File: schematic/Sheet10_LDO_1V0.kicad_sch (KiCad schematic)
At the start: 8 parts, among them U8 TPS7H1111-SP

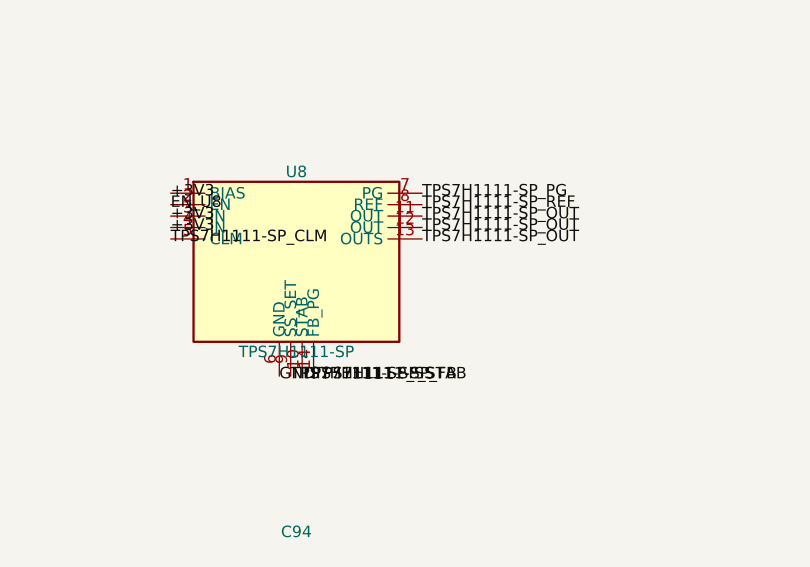
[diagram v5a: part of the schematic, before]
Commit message: fix: isolate ISL70003ASEH buck pins, fix LMX_SYNC collision, NC pins, connector pin names
- ISL70003ASEH pins now use ref prefix (U6_LX1 vs U7_LX1) to prevent shorts
- Buck SYNC pins separated from LMX_SYNC (power sync ≠ PLL sync)
- NC pins properly skipped (unconnected)
- Connector PIN_1..PIN_6 use ref prefix (J1_PIN_1 vs J2_PIN_1)
- Fixed annotation warnings in Sheet13 (C_dev→C125, R_dev→R74, U_TPS7H→U14)
- Regenerated all PDFs and SVGs
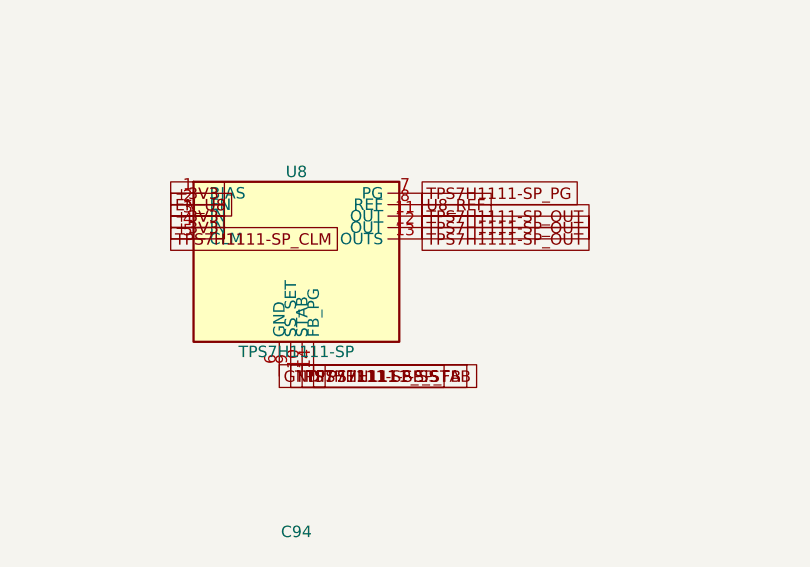
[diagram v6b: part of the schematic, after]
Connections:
- net TPS7H1111-SP_REF renamed U8_REF
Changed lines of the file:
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@@
     (pin "2")
   )
-  (label "+3V3" (at 186.0300 72.3800 0) (effects (font (size 1.27 1.27))))
-  (label "EN_U8" (at 186.0300 73.6500 0) (effects (font (size 1.27 1.27))))
-  (label "+3V3" (at 186.0300 74.9200 0) (effects (font (size 1.27 1.27))))
-  (label "+3V3" (at 186.0300 76.1900 0) (effects (font (size 1.27 1.27))))
-  (label "TPS7H1111-SP_CLM" (at 186.0300 77.4600 0) (effects (font (size 1.27 1.27))))
-  (label "TPS7H1111-SP_PG" (at 213.9700 72.3800 0) (effects (font (size 1.27 1.27))))
-  (label "TPS7H1111-SP_REF" (at 213.9700 73.6500 0) (effects (font (size 1.27 1.27))))
-  (label "TPS7H1111-SP_OUT" (at 213.9700 74.9200 0) (effects (font (size 1.27 1.27))))
-  (label "TPS7H1111-SP_OUT" (at 213.9700 76.1900 0) (effects (font (size 1.27 1.27))))
-  (label "TPS7H1111-SP_OUT" (at 213.9700 77.4600 0) (effects (font (size 1.27 1.27))))
-  (label "GND" (at 198.0950 92.7000 0) (effects (font (size 1.27 1.27))))
-  (label "TPS7H1111-SP_SS" (at 199.3650 92.7000 0) (effects (font (size 1.27 1.27))))
-  (label "TPS7H1111-SP_STAB" (at 200.6350 92.7000 0) (effects (font (size 1.27 1.27))))
-  (label "TPS7H1111-SP_FB" (at 201.9050 92.7000 0) (effects (font (size 1.27 1.27))))
+  (global_label "+3V3" (at 186.0300 72.3800 0) (effects (font (size 1.27 1.27))))
+  (global_label "EN_U8" (at 186.0300 73.6500 0) (effects (font (size 1.27 1.27))))
+  (global_label "+3V3" (at 186.0300 74.9200 0) (effects (font (size 1.27 1.27))))
+  (global_label "+3V3" (at 186.0300 76.1900 0) (effects (font (size 1.27 1.27))))
+  (global_label "TPS7H1111-SP_CLM" (at 186.0300 77.4600 0) (effects (font (size 1.27 1.27))))
+  (global_label "TPS7H1111-SP_PG" (at 213.9700 72.3800 0) (effects (font (size 1.27 1.27))))
+  (global_label "U8_REF" (at 213.9700 73.6500 0) (effects (font (size 1.27 1.27))))
+  (global_label "TPS7H1111-SP_OUT" (at 213.9700 74.9200 0) (effects (font (size 1.27 1.27))))
+  (global_label "TPS7H1111-SP_OUT" (at 213.9700 76.1900 0) (effects (font (size 1.27 1.27))))
+  (global_label "TPS7H1111-SP_OUT" (at 213.9700 77.4600 0) (effects (font (size 1.27 1.27))))
+  (global_label "GND" (at 198.0950 92.7000 0) (effects (font (size 1.27 1.27))))
+  (global_label "TPS7H1111-SP_SS" (at 199.3650 92.7000 0) (effects (font (size 1.27 1.27))))
+  (global_label "TPS7H1111-SP_STAB" (at 200.6350 92.7000 0) (effects (font (size 1.27 1.27))))
+  (global_label "TPS7H1111-SP_FB" (at 201.9050 92.7000 0) (effects (font (size 1.27 1.27))))
   (sheet_instances (path "/" (page "1")))
 )

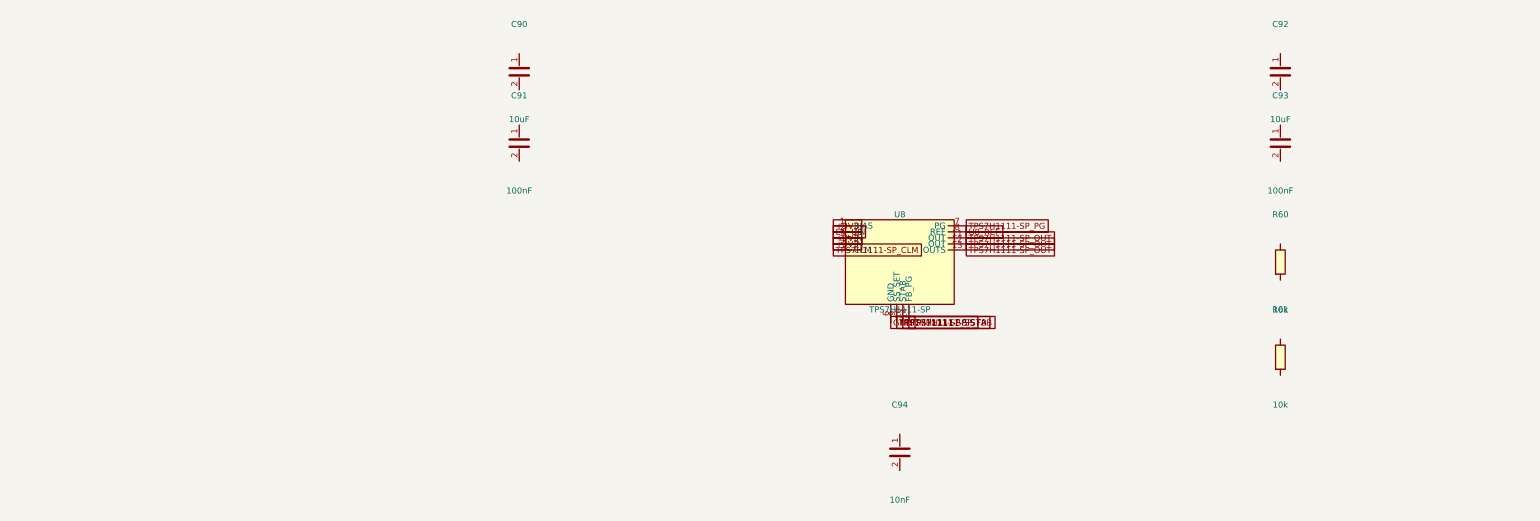
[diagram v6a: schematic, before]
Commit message: feat: connect ALL passive components and fix clock routing
- Added PASSIVE_TOPOLOGY dict mapping 139 passives to their nets
- Passive pin endpoints now get global_labels (was 0 connected, now 138)
- R38 intentionally GND-GND (RECAL_EN pull-down)
- Fixed LMK clock output mapping: CLKout0→ADC_CLK_P, CLKout2→FPGA_REFCLK_P, etc.
- Fixed TPS7H5001-SP SYNC pin collision with LMX_SYNC
- Total connections: 867 pins (up from 641)
- Cross-sheet nets: 52
- Power rails: VIN(33), +3V3(98), GND(228) all with decoupling
- JESD204C: U1↔U2 on 4 lanes ✓
- SPI: U1↔U2↔U3↔U4 ✓
- Clock: LMK→ADC (CLK+SYSREF), LMK→FPGA (REF+SPW) ✓
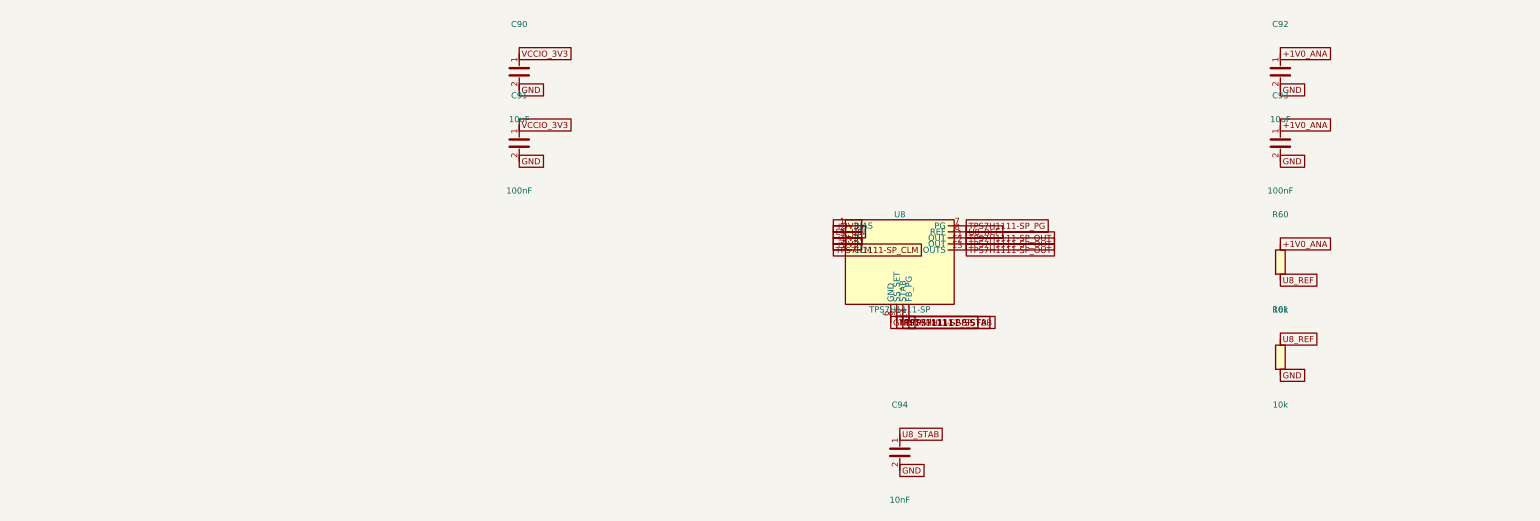
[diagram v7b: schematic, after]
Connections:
- net GND: now also C90.2, C91.2, C92.2, C93.2, C94.2, R61.2
- net U8_REF: now also R60.2, R61.1
- net VCCIO_3V3: now reaches C91.1
- net VCCIO_3V3: now also C90.1
- net +1V0_ANA: now reaches R60.1
- net +1V0_ANA: now also C92.1, C93.1
- net U8_STAB: now reaches C94.1
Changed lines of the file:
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@@
   (global_label "TPS7H1111-SP_STAB" (at 200.6350 92.7000 0) (effects (font (size 1.27 1.27))))
   (global_label "TPS7H1111-SP_FB" (at 201.9050 92.7000 0) (effects (font (size 1.27 1.27))))
+  (global_label "VCCIO_3V3" (at 120.0000 36.1900 0) (effects (font (size 1.27 1.27))))
+  (global_label "GND" (at 120.0000 43.8100 0) (effects (font (size 1.27 1.27))))
+  (global_label "VCCIO_3V3" (at 120.0000 51.1900 0) (effects (font (size 1.27 1.27))))
+  (global_label "GND" (at 120.0000 58.8100 0) (effects (font (size 1.27 1.27))))
+  (global_label "+1V0_ANA" (at 280.0000 36.1900 0) (effects (font (size 1.27 1.27))))
+  (global_label "GND" (at 280.0000 43.8100 0) (effects (font (size 1.27 1.27))))
+  (global_label "+1V0_ANA" (at 280.0000 51.1900 0) (effects (font (size 1.27 1.27))))
+  (global_label "GND" (at 280.0000 58.8100 0) (effects (font (size 1.27 1.27))))
+  (global_label "U8_STAB" (at 200.0000 116.1900 0) (effects (font (size 1.27 1.27))))
+  (global_label "GND" (at 200.0000 123.8100 0) (effects (font (size 1.27 1.27))))
+  (global_label "+1V0_ANA" (at 280.0000 76.1900 0) (effects (font (size 1.27 1.27))))
+  (global_label "U8_REF" (at 280.0000 83.8100 0) (effects (font (size 1.27 1.27))))
+  (global_label "U8_REF" (at 280.0000 96.1900 0) (effects (font (size 1.27 1.27))))
+  (global_label "GND" (at 280.0000 103.8100 0) (effects (font (size 1.27 1.27))))
   (sheet_instances (path "/" (page "1")))
 )
